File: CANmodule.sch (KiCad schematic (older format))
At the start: 14 parts

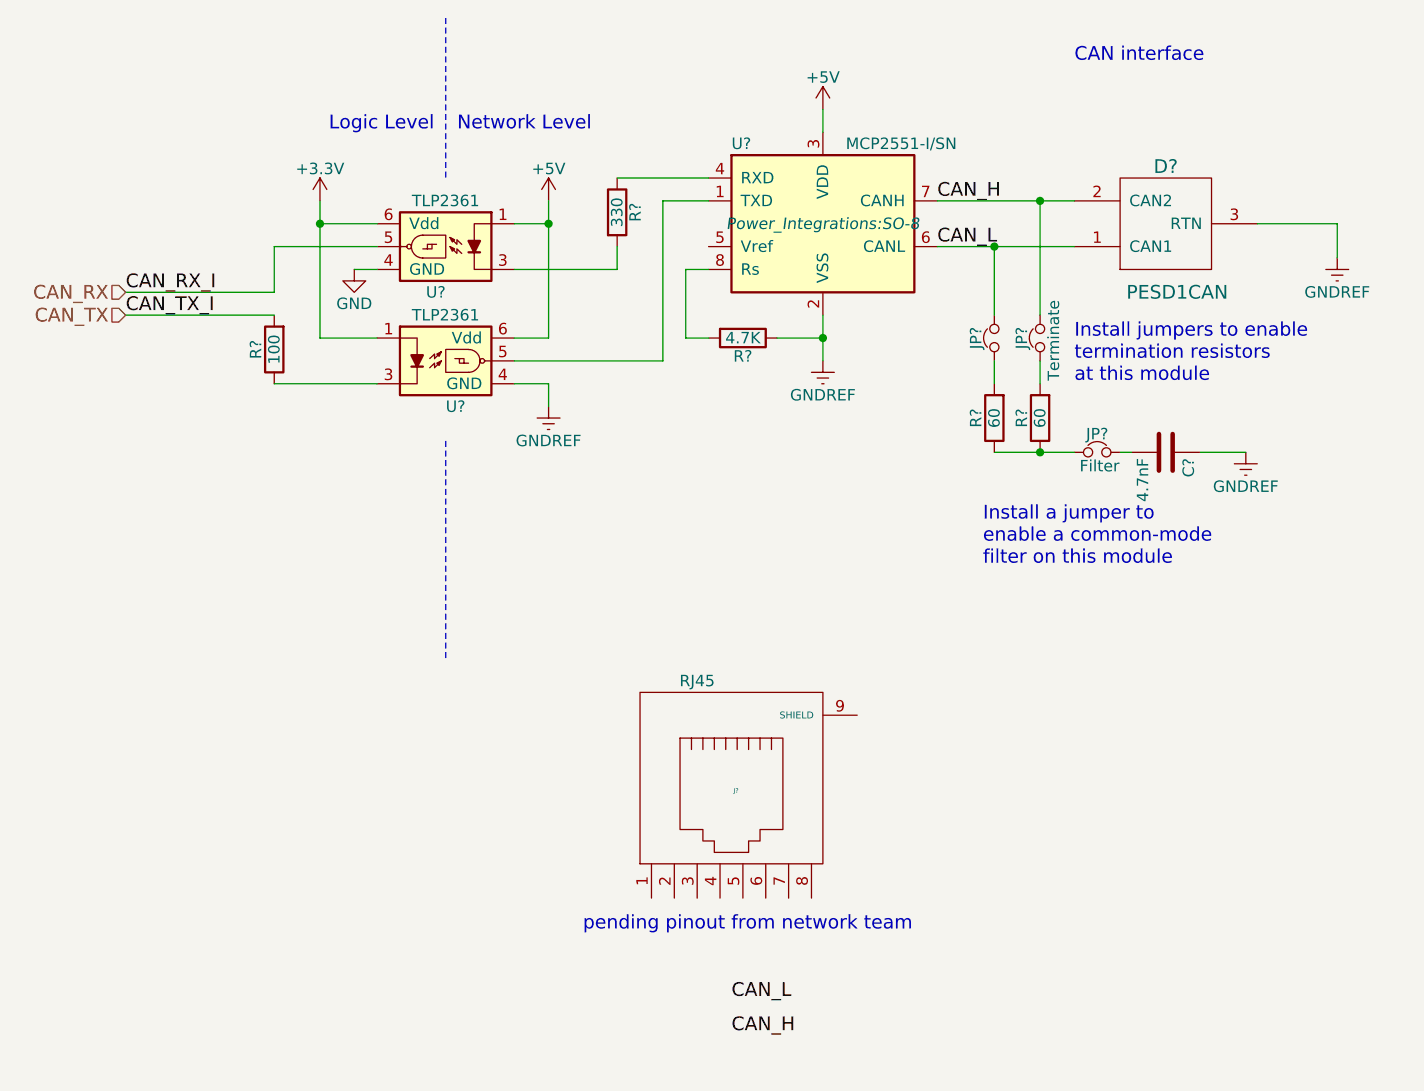
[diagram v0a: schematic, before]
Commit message: added digital pot
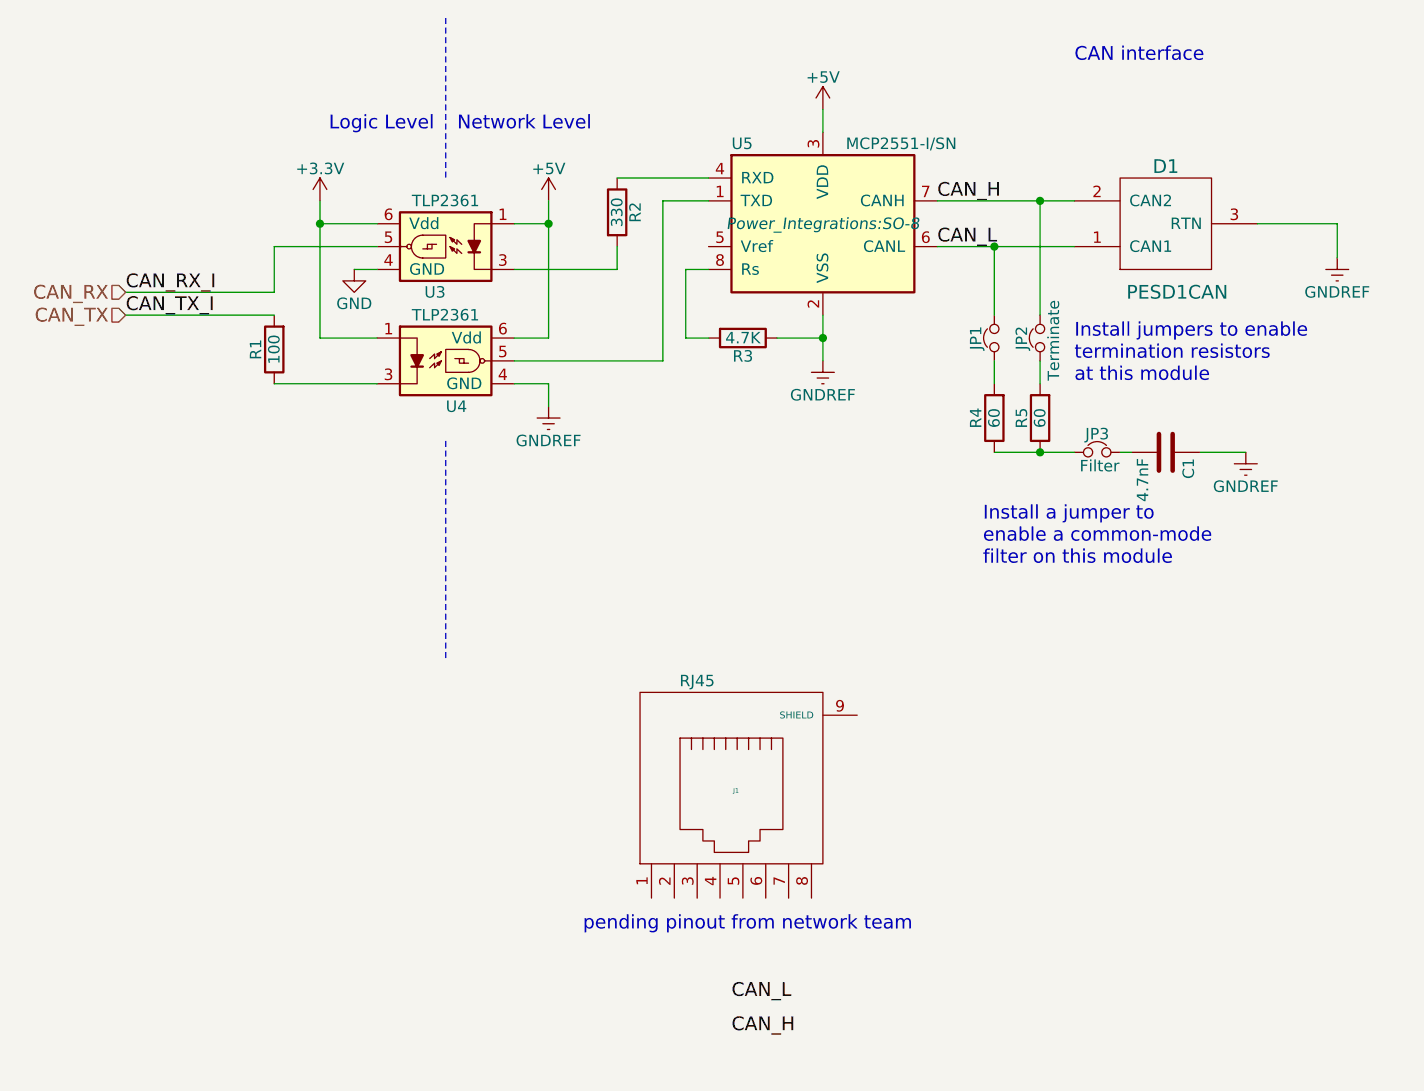
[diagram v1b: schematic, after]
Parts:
- gave numbers to parts that had none: 14
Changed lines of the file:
@@
 $EndDescr
 $Comp
-L R R?
+L R R3
 U 1 1 57FCAEE8
 P 6850 2000
-F 0 "R?" V 6930 2000 50  0000 C CNN
+F 0 "R3" V 6930 2000 50  0000 C CNN
 F 1 "4.7K" V 6850 2000 50  0000 C CNN
 F 2 "Resistors_SMD:R_0603" V 6780 2000 50  0001 C CNN
@@
 $EndComp
 $Comp
-L C C?
+L C C1
 U 1 1 57FCAEE9
 P 8700 2500
-F 0 "C?" H 8725 2600 50  0000 L CNN
+F 0 "C1" H 8725 2600 50  0000 L CNN
 F 1 "4.7nF" H 8725 2400 50  0000 L CNN
 F 2 "Capacitors_SMD:C_1206" H 8738 2350 50  0001 C CNN
@@
 $EndComp
 $Comp
-L R R?
+L R R4
 U 1 1 57FCAEEA
 P 7950 2350
-F 0 "R?" V 8030 2350 50  0000 C CNN
+F 0 "R4" V 8030 2350 50  0000 C CNN
 F 1 "60" V 7950 2350 50  0000 C CNN
 F 2 "Resistors_SMD:R_1210" V 7880 2350 50  0001 C CNN
@@
 $EndComp
 $Comp
-L R R?
+L R R5
 U 1 1 57FCAEEB
 P 8150 2350
-F 0 "R?" V 8230 2350 50  0000 C CNN
+F 0 "R5" V 8230 2350 50  0000 C CNN
 F 1 "60" V 8150 2350 50  0000 C CNN
 F 2 "Resistors_SMD:R_1210" V 8080 2350 50  0001 C CNN
@@
 $EndComp
 $Comp
-L GNDREF #PWR?
+L GNDREF #PWR7
 U 1 1 57FCAEEC
 P 9050 2500
-F 0 "#PWR?" H 9050 2250 50  0001 C CNN
+F 0 "#PWR7" H 9050 2250 50  0001 C CNN
 F 1 "GNDREF" H 9050 2350 50  0000 C CNN
 F 2 "" H 9050 2500 50  0000 C CNN
@@
 $EndComp
 $Comp
-L GNDREF #PWR?
+L GNDREF #PWR8
 U 1 1 57FCAEED
 P 9450 1650
-F 0 "#PWR?" H 9450 1400 50  0001 C CNN
+F 0 "#PWR8" H 9450 1400 50  0001 C CNN
 F 1 "GNDREF" H 9450 1500 50  0000 C CNN
 F 2 "" H 9450 1650 50  0000 C CNN
@@
 $EndComp
 $Comp
-L GNDREF #PWR?
+L GNDREF #PWR6
 U 1 1 57FCAEEE
 P 7200 2100
-F 0 "#PWR?" H 7200 1850 50  0001 C CNN
+F 0 "#PWR6" H 7200 1850 50  0001 C CNN
 F 1 "GNDREF" H 7200 1950 50  0000 C CNN
 F 2 "" H 7200 2100 50  0000 C CNN
@@
 $EndComp
 $Comp
-L +3.3V #PWR?
+L +3.3V #PWR1
 U 1 1 57FCAEEF
 P 5000 1400
-F 0 "#PWR?" H 5000 1250 50  0001 C CNN
+F 0 "#PWR1" H 5000 1250 50  0001 C CNN
 F 1 "+3.3V" H 5000 1540 50  0000 C CNN
 F 2 "" H 5000 1400 50  0000 C CNN
@@
 $EndComp
 $Comp
-L +5V #PWR?
+L +5V #PWR3
 U 1 1 57FCAEF0
 P 6000 1400
-F 0 "#PWR?" H 6000 1250 50  0001 C CNN
+F 0 "#PWR3" H 6000 1250 50  0001 C CNN
 F 1 "+5V" H 6000 1540 50  0000 C CNN
 F 2 "" H 6000 1400 50  0000 C CNN
@@
 $EndComp
 $Comp
-L +5V #PWR?
+L +5V #PWR5
 U 1 1 57FCAEF1
 P 7200 1000
-F 0 "#PWR?" H 7200 850 50  0001 C CNN
+F 0 "#PWR5" H 7200 850 50  0001 C CNN
 F 1 "+5V" H 7200 1140 50  0000 C CNN
 F 2 "" H 7200 1000 50  0000 C CNN
@@
 CAN_L
 $Comp
-L R R?
+L R R2
 U 1 1 57FCAEF2
 P 6300 1450
-F 0 "R?" V 6380 1450 50  0000 C CNN
+F 0 "R2" V 6380 1450 50  0000 C CNN
 F 1 "330" V 6300 1450 50  0000 C CNN
 F 2 "Resistors_SMD:R_0603" V 6230 1450 50  0001 C CNN
@@
 $EndComp
 $Comp
-L Jumper_NC_Small JP?
+L Jumper_NC_Small JP1
 U 1 1 57FCAEF3
 P 7950 2000
-F 0 "JP?" H 7950 2080 50  0000 C CNN
+F 0 "JP1" H 7950 2080 50  0000 C CNN
 F 1 "Terminate" H 7960 1940 50  0001 C CNN
 F 2 "LocalLib:JumperSingle" H 7950 2000 50  0001 C CNN
@@
 $EndComp
 $Comp
-L Jumper_NC_Small JP?
+L Jumper_NC_Small JP2
 U 1 1 57FCAEF4
 P 8150 2000
-F 0 "JP?" H 8150 2080 50  0000 C CNN
+F 0 "JP2" H 8150 2080 50  0000 C CNN
 F 1 "Terminate" H 8160 1940 50  0000 C CNN
 F 2 "LocalLib:JumperSingle" H 8150 2000 50  0001 C CNN
@@
 $EndComp
 $Comp
-L Jumper_NC_Small JP?
+L Jumper_NC_Small JP3
 U 1 1 57FCAEF5
 P 8400 2500
-F 0 "JP?" H 8400 2580 50  0000 C CNN
+F 0 "JP3" H 8400 2580 50  0000 C CNN
 F 1 "Filter" H 8410 2440 50  0000 C CNN
 F 2 "LocalLib:JumperSingle" H 8400 2500 50  0001 C CNN
@@
 $EndComp
 $Comp
-L R R?
+L R R1
 U 1 1 57FCAEF6
 P 4800 2050
-F 0 "R?" V 4880 2050 50  0000 C CNN
+F 0 "R1" V 4880 2050 50  0000 C CNN
 F 1 "100" V 4800 2050 50  0000 C CNN
 F 2 "Resistors_SMD:R_0603" V 4730 2050 50  0001 C CNN
@@
 $EndComp
 $Comp
-L GND #PWR?
+L GND #PWR2
 U 1 1 57FCAEF7
 P 5150 1700
-F 0 "#PWR?" H 5150 1450 50  0001 C CNN
+F 0 "#PWR2" H 5150 1450 50  0001 C CNN
 F 1 "GND" H 5150 1550 50  0000 C CNN
 F 2 "" H 5150 1700 50  0000 C CNN
@@
 $EndComp
 $Comp
-L TLP2361 U?
+L TLP2361 U4
 U 1 1 57FCAEF8
 P 5550 2100
-F 0 "U?" H 5550 1900 50  0000 L CNN
+F 0 "U4" H 5550 1900 50  0000 L CNN
 F 1 "TLP2361" H 5550 2300 50  0000 C CNN
 F 2 "LocalLib:soic-5" H 5350 1900 50  0001 L CIN
@@
 $EndComp
 $Comp
-L TLP2361 U?
+L TLP2361 U3
 U 1 1 57FCAEF9
 P 5550 1600
-F 0 "U?" H 5550 1400 50  0000 L CNN
+F 0 "U3" H 5550 1400 50  0000 L CNN
 F 1 "TLP2361" H 5550 1800 50  0000 C CNN
 F 2 "LocalLib:soic-5" H 5350 1400 50  0001 L CIN
@@
 CAN interface
 $Comp
-L PESD1CAN D?
+L PESD1CAN D1
 U 1 1 57FCAEFA
 P 8700 1500
-F 0 "D?" H 8700 1250 60  0000 C CNN
+F 0 "D1" H 8700 1250 60  0000 C CNN
 F 1 "PESD1CAN" H 8650 1800 60  0000 C CNN
 F 2 "TO_SOT_Packages_SMD:SOT-23_Handsoldering" H 8700 1500 60  0001 C CNN
@@
 $EndComp
 $Comp
-L MCP2551-I/SN U?
+L MCP2551-I/SN U5
 U 1 1 57FCAEFB
 P 7200 1500
-F 0 "U?" H 6800 1850 50  0000 L CNN
+F 0 "U5" H 6800 1850 50  0000 L CNN
 F 1 "MCP2551-I/SN" H 7300 1850 50  0000 L CNN
 F 2 "Power_Integrations:SO-8" H 7200 1500 50  0000 C CIN
@@
 $EndComp
 $Comp
-L GNDREF #PWR?
+L GNDREF #PWR4
 U 1 1 57FCAEFC
 P 6000 2300
-F 0 "#PWR?" H 6000 2050 50  0001 C CNN
+F 0 "#PWR4" H 6000 2050 50  0001 C CNN
 F 1 "GNDREF" H 6000 2150 50  0000 C CNN
 F 2 "" H 6000 2300 50  0000 C CNN
@@
 CAN_RX
 $Comp
-L RJ45 J?
+L RJ45 J1
 U 1 1 57FCC775
 P 6800 4000
-F 0 "J?" H 6820 4020 20  0000 C CNN
+F 0 "J1" H 6820 4020 20  0000 C CNN
 F 1 "RJ45" H 6650 4500 50  0000 C CNN
 F 2 "" H 6800 4000 50  0000 C CNN

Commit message: Added TE 23pins and netlist
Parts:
- J1: footprint (none) -> Connect:RJ45_8
- JP1, JP2, JP3: footprint LocalLib:JumperSingle -> electric_car_lib:JumperSingle
- R1, R2, R3: footprint Resistors_SMD:R_0603 -> Resistors_SMD:R_1210_HandSoldering
- R4, R5: footprint Resistors_SMD:R_1210 -> Resistors_SMD:R_1210_HandSoldering
- U3, U4: footprint LocalLib:soic-5 -> electric_car_lib:soic-5
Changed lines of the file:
@@
 LIBS:contrib
 LIBS:valves
-LIBS:electric_car
 LIBS:Motor-interface-cache
 EELAYER 25 0
@@
 F 0 "R3" V 6930 2000 50  0000 C CNN
 F 1 "4.7K" V 6850 2000 50  0000 C CNN
-F 2 "Resistors_SMD:R_0603" V 6780 2000 50  0001 C CNN
+F 2 "Resistors_SMD:R_1210_HandSoldering" V 6780 2000 50  0001 C CNN
 F 3 "" H 6850 2000 50  0000 C CNN
 	1    6850 2000
@@
 F 0 "R4" V 8030 2350 50  0000 C CNN
 F 1 "60" V 7950 2350 50  0000 C CNN
-F 2 "Resistors_SMD:R_1210" V 7880 2350 50  0001 C CNN
+F 2 "Resistors_SMD:R_1210_HandSoldering" V 7880 2350 50  0001 C CNN
 F 3 "" H 7950 2350 50  0000 C CNN
 	1    7950 2350
@@
 F 0 "R5" V 8230 2350 50  0000 C CNN
 F 1 "60" V 8150 2350 50  0000 C CNN
-F 2 "Resistors_SMD:R_1210" V 8080 2350 50  0001 C CNN
+F 2 "Resistors_SMD:R_1210_HandSoldering" V 8080 2350 50  0001 C CNN
 F 3 "" H 8150 2350 50  0000 C CNN
 	1    8150 2350
@@
 $EndComp
 $Comp
-L GNDREF #PWR7
+L GNDREF #PWR07
 U 1 1 57FCAEEC
 P 9050 2500
-F 0 "#PWR7" H 9050 2250 50  0001 C CNN
+F 0 "#PWR07" H 9050 2250 50  0001 C CNN
 F 1 "GNDREF" H 9050 2350 50  0000 C CNN
 F 2 "" H 9050 2500 50  0000 C CNN
@@
 $EndComp
 $Comp
-L GNDREF #PWR8
+L GNDREF #PWR08
 U 1 1 57FCAEED
 P 9450 1650
-F 0 "#PWR8" H 9450 1400 50  0001 C CNN
+F 0 "#PWR08" H 9450 1400 50  0001 C CNN
 F 1 "GNDREF" H 9450 1500 50  0000 C CNN
 F 2 "" H 9450 1650 50  0000 C CNN
@@
 $EndComp
 $Comp
-L GNDREF #PWR6
+L GNDREF #PWR09
 U 1 1 57FCAEEE
 P 7200 2100
-F 0 "#PWR6" H 7200 1850 50  0001 C CNN
+F 0 "#PWR09" H 7200 1850 50  0001 C CNN
 F 1 "GNDREF" H 7200 1950 50  0000 C CNN
 F 2 "" H 7200 2100 50  0000 C CNN
@@
 $EndComp
 $Comp
-L +3.3V #PWR1
+L +3.3V #PWR010
 U 1 1 57FCAEEF
 P 5000 1400
-F 0 "#PWR1" H 5000 1250 50  0001 C CNN
+F 0 "#PWR010" H 5000 1250 50  0001 C CNN
 F 1 "+3.3V" H 5000 1540 50  0000 C CNN
 F 2 "" H 5000 1400 50  0000 C CNN
@@
 $EndComp
 $Comp
-L +5V #PWR3
+L +5V #PWR011
 U 1 1 57FCAEF0
 P 6000 1400
-F 0 "#PWR3" H 6000 1250 50  0001 C CNN
+F 0 "#PWR011" H 6000 1250 50  0001 C CNN
 F 1 "+5V" H 6000 1540 50  0000 C CNN
 F 2 "" H 6000 1400 50  0000 C CNN
@@
 $EndComp
 $Comp
-L +5V #PWR5
+L +5V #PWR012
 U 1 1 57FCAEF1
 P 7200 1000
-F 0 "#PWR5" H 7200 850 50  0001 C CNN
+F 0 "#PWR012" H 7200 850 50  0001 C CNN
 F 1 "+5V" H 7200 1140 50  0000 C CNN
 F 2 "" H 7200 1000 50  0000 C CNN
@@
 F 0 "R2" V 6380 1450 50  0000 C CNN
 F 1 "330" V 6300 1450 50  0000 C CNN
-F 2 "Resistors_SMD:R_0603" V 6230 1450 50  0001 C CNN
+F 2 "Resistors_SMD:R_1210_HandSoldering" V 6230 1450 50  0001 C CNN
 F 3 "" H 6300 1450 50  0000 C CNN
 	1    6300 1450
@@
 F 0 "JP1" H 7950 2080 50  0000 C CNN
 F 1 "Terminate" H 7960 1940 50  0001 C CNN
-F 2 "LocalLib:JumperSingle" H 7950 2000 50  0001 C CNN
+F 2 "electric_car_lib:JumperSingle" H 7950 2000 50  0001 C CNN
 F 3 "" H 7950 2000 50  0000 C CNN
 	1    7950 2000
@@
 F 0 "JP2" H 8150 2080 50  0000 C CNN
 F 1 "Terminate" H 8160 1940 50  0000 C CNN
-F 2 "LocalLib:JumperSingle" H 8150 2000 50  0001 C CNN
+F 2 "electric_car_lib:JumperSingle" H 8150 2000 50  0001 C CNN
 F 3 "" H 8150 2000 50  0000 C CNN
 	1    8150 2000
@@
 F 0 "JP3" H 8400 2580 50  0000 C CNN
 F 1 "Filter" H 8410 2440 50  0000 C CNN
-F 2 "LocalLib:JumperSingle" H 8400 2500 50  0001 C CNN
+F 2 "electric_car_lib:JumperSingle" H 8400 2500 50  0001 C CNN
 F 3 "" H 8400 2500 50  0000 C CNN
 	1    8400 2500
@@
 F 0 "R1" V 4880 2050 50  0000 C CNN
 F 1 "100" V 4800 2050 50  0000 C CNN
-F 2 "Resistors_SMD:R_0603" V 4730 2050 50  0001 C CNN
+F 2 "Resistors_SMD:R_1210_HandSoldering" V 4730 2050 50  0001 C CNN
 F 3 "" H 4800 2050 50  0000 C CNN
 	1    4800 2050
@@
 $EndComp
 $Comp
-L GND #PWR2
+L GND #PWR013
 U 1 1 57FCAEF7
 P 5150 1700
-F 0 "#PWR2" H 5150 1450 50  0001 C CNN
+F 0 "#PWR013" H 5150 1450 50  0001 C CNN
 F 1 "GND" H 5150 1550 50  0000 C CNN
 F 2 "" H 5150 1700 50  0000 C CNN
@@
 F 0 "U4" H 5550 1900 50  0000 L CNN
 F 1 "TLP2361" H 5550 2300 50  0000 C CNN
-F 2 "LocalLib:soic-5" H 5350 1900 50  0001 L CIN
+F 2 "electric_car_lib:soic-5" H 5350 1900 50  0001 L CIN
 F 3 "" H 5550 2100 50  0000 L CNN
 	1    5550 2100
@@
 F 0 "U3" H 5550 1400 50  0000 L CNN
 F 1 "TLP2361" H 5550 1800 50  0000 C CNN
-F 2 "LocalLib:soic-5" H 5350 1400 50  0001 L CIN
+F 2 "electric_car_lib:soic-5" H 5350 1400 50  0001 L CIN
 F 3 "" H 5550 1600 50  0000 L CNN
 	1    5550 1600
@@
 $EndComp
 $Comp
-L GNDREF #PWR4
+L GNDREF #PWR014
 U 1 1 57FCAEFC
 P 6000 2300
-F 0 "#PWR4" H 6000 2050 50  0001 C CNN
+F 0 "#PWR014" H 6000 2050 50  0001 C CNN
 F 1 "GNDREF" H 6000 2150 50  0000 C CNN
 F 2 "" H 6000 2300 50  0000 C CNN
@@
 F 0 "J1" H 6820 4020 20  0000 C CNN
 F 1 "RJ45" H 6650 4500 50  0000 C CNN
-F 2 "" H 6800 4000 50  0000 C CNN
+F 2 "Connect:RJ45_8" H 6800 4000 50  0001 C CNN
 F 3 "" H 6800 4000 50  0000 C CNN
 	1    6800 4000
